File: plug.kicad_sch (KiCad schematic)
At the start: 27 parts, among them J1 KF2EDGR-3.81-2P, J10 Conn_01x02_XH2.54, J11 Conn_01x04_GH1.25, J3 KF2EDGR-3.81-2P, J4 KF2EDGR-3.81-2P, J5 Conn_01x04_GH1.25, J6 Conn_01x04_GH1.25, J7 Conn_01x02_XH2.54, J8 Conn_01x02_XH2.54, J9 Conn_01x02_XH2.54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

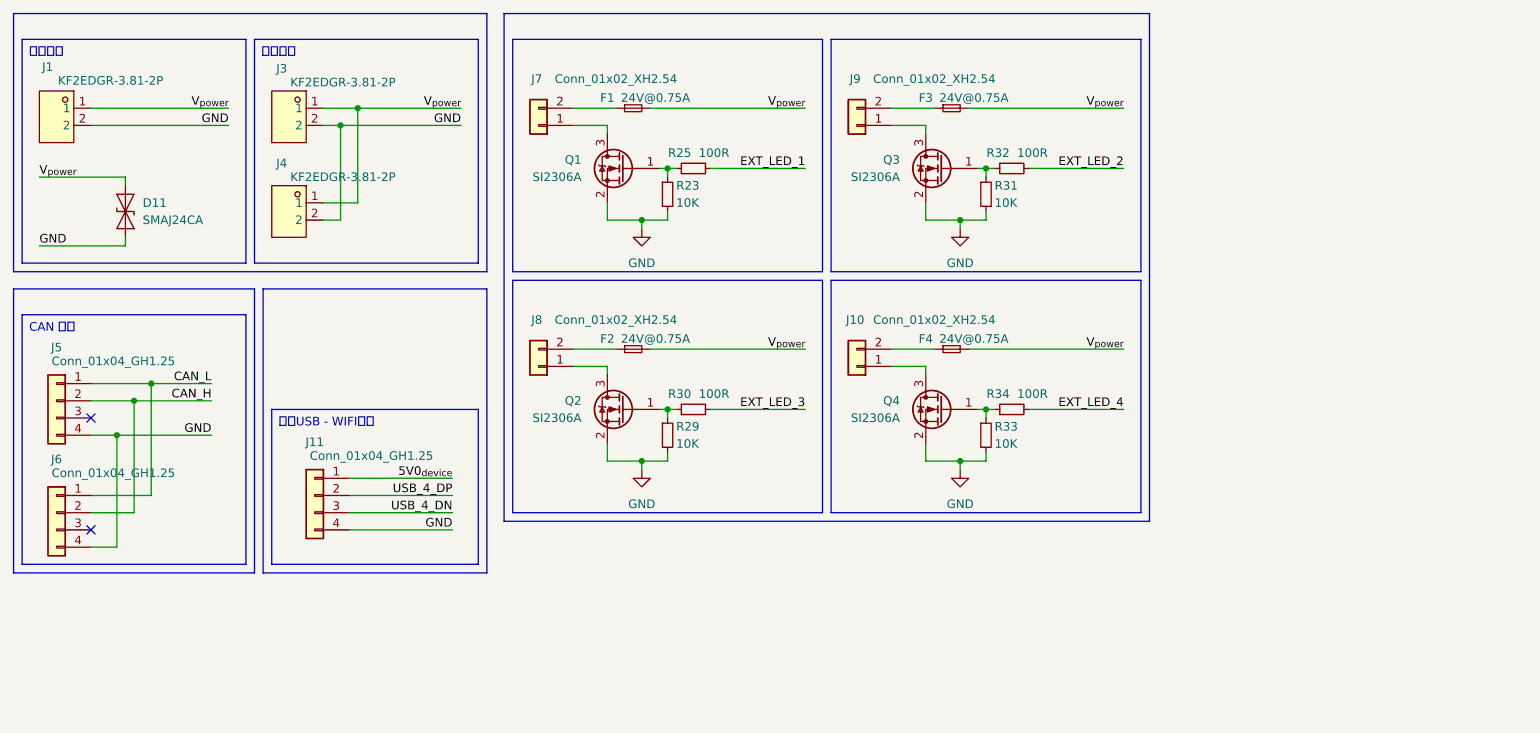
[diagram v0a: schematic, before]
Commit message: 暂存: 基本完成原理图(未分配封装，未ERC)
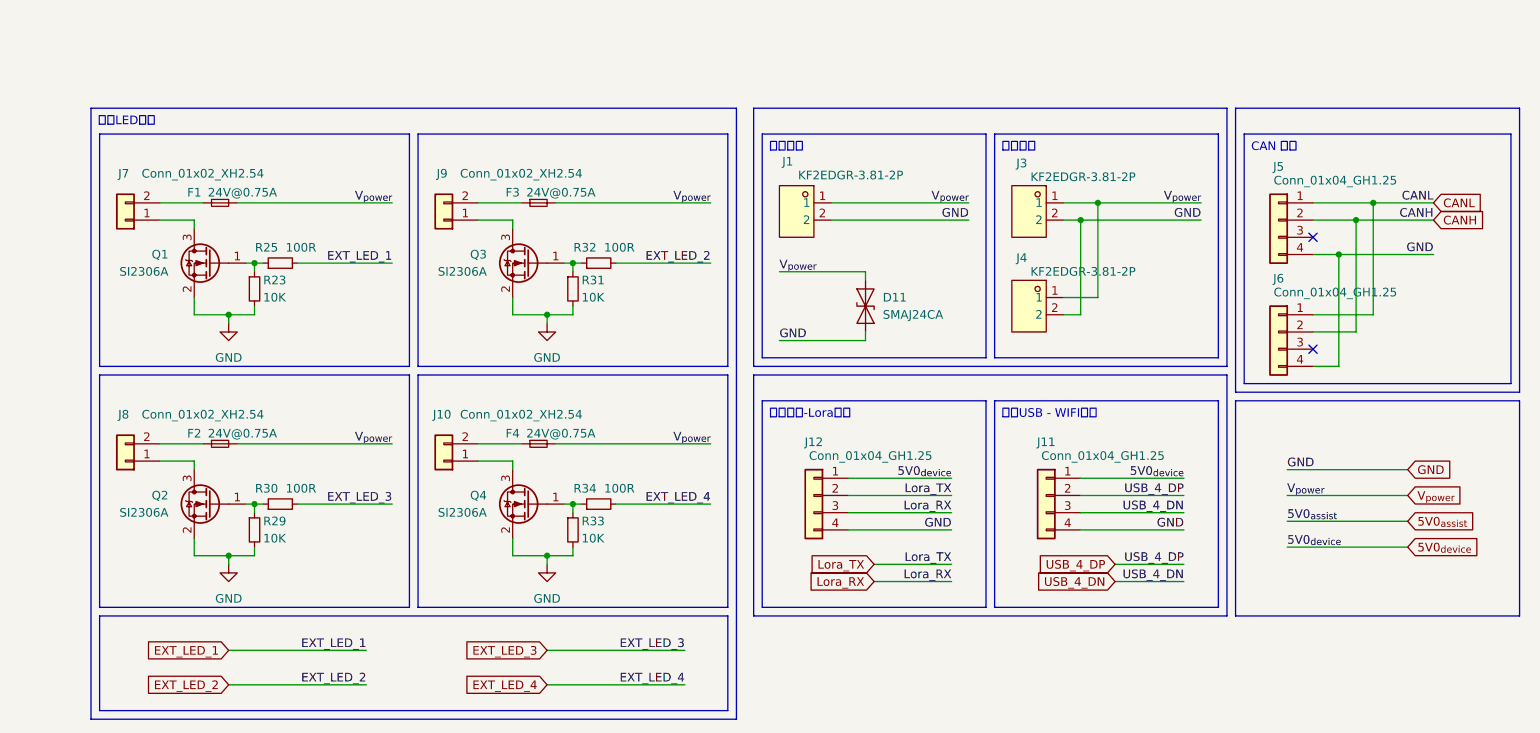
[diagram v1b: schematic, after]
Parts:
- added J12: Conn_01x04_GH1.25, symbol Connector_Generic:Conn_01x04
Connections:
- net 5V0_{device}: now also J12.1 (Pin_1)
- net GND: now also J12.4 (Pin_4)
- net CAN_H renamed CANH
- net CAN_L renamed CANL
- new net Lora_RX: J12.3 (Pin_3)
- new net Lora_TX: J12.2 (Pin_2)
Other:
- moved on the sheet: D11, F1, F2, F3, F4, J1, J10, J11, J3, J4, J5, J6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

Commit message: 暂存: 基本完成原理图(差雷达接口)
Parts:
- F1, F2, F3, F4: footprint (none) -> Fuse:Fuse_1812_4532Metric
- J10: renamed from J11; footprint (none) -> Connector_JST:JST_GH_SM04B-GHS-TB_1x04-1MP_P1.25mm_Horizontal
- J11: renamed from J5; footprint (none) -> Connector_JST:JST_GH_SM04B-GHS-TB_1x04-1MP_P1.25mm_Horizontal
- J12: renamed from J6; footprint (none) -> Connector_JST:JST_GH_SM04B-GHS-TB_1x04-1MP_P1.25mm_Horizontal
- J2: renamed from J7; footprint (none) -> Connector_JST:JST_XH_S2B-XH-A-1_1x02_P2.50mm_Horizontal
- J3: renamed from J8; footprint (none) -> Connector_JST:JST_XH_S2B-XH-A-1_1x02_P2.50mm_Horizontal
- J4: renamed from J9; footprint (none) -> Connector_JST:JST_XH_S2B-XH-A-1_1x02_P2.50mm_Horizontal
- J5: renamed from J10; footprint (none) -> Connector_JST:JST_XH_S2B-XH-A-1_1x02_P2.50mm_Horizontal
- J7: renamed from J12; footprint (none) -> Connector_JST:JST_GH_SM04B-GHS-TB_1x04-1MP_P1.25mm_Horizontal
- R26: renamed from R23; footprint (none) -> Resistor_SMD:R_0402_1005Metric
- R27: renamed from R29; footprint (none) -> Resistor_SMD:R_0402_1005Metric
- R28: renamed from R25; footprint (none) -> Resistor_SMD:R_0402_1005Metric
- R29: renamed from R30; footprint (none) -> Resistor_SMD:R_0402_1005Metric
- R30: renamed from R31; footprint (none) -> Resistor_SMD:R_0402_1005Metric
- R31: renamed from R33; footprint (none) -> Resistor_SMD:R_0402_1005Metric
- R32: footprint (none) -> Resistor_SMD:R_0402_1005Metric
- R33: renamed from R34; footprint (none) -> Resistor_SMD:R_0402_1005Metric
- renumbered J1 to J6, J3 to J8, J4 to J9
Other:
- note added: "补雷达接口及标签！！！"
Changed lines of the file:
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@@
+		)
+	)
+	(text "补雷达接口及标签！！！"
+		(exclude_from_sim no)
+		(at 49.53 32.004 0)
+		(effects
+			(font
+				(size 2.54 2.54)
+				(thickness 0.3175)
+				(color 255 0 0 1)
+			)
 		)
 	)
@@
 		(on_board yes)
 		(dnp no)
-		(property "Reference" "J6"
+		(property "Reference" "J12"
 			(at 205.74 60.706 0)
 			(effects
@@
 			)
 		)
-		(property "Footprint" ""
+		(property "Footprint" "Connector_JST:JST_GH_SM04B-GHS-TB_1x04-1MP_P1.25mm_Horizontal"
 			(at 205.74 68.58 0)
 			(effects
@@
 			(project "ZW1S"
 				(path "/c658c753-a869-4eb9-a520-6b2e7fae7fd9/cfdc2bd0-e52f-4e45-9f57-35a106e1bb09"
-					(reference "J6")
+					(reference "J12")
 					(unit 1)
 				)
@@
 		(dnp no)
 		(fields_autoplaced yes)
-		(property "Reference" "#PWR7"
+		(property "Reference" "#PWR13"
 			(at 50.8 73.66 0)
 			(effects
@@
 			(project ""
 				(path "/c658c753-a869-4eb9-a520-6b2e7fae7fd9/cfdc2bd0-e52f-4e45-9f57-35a106e1bb09"
-					(reference "#PWR7")
+					(reference "#PWR13")
 					(unit 1)
 				)
@@
 		(on_board yes)
 		(dnp no)
-		(property "Reference" "J7"
+		(property "Reference" "J2"
 			(at 35.306 45.212 0)
 			(effects
@@
 			)
 		)
-		(property "Footprint" ""
+		(property "Footprint" "Connector_JST:JST_XH_S2B-XH-A-1_1x02_P2.50mm_Horizontal"
 			(at 35.56 52.07 0)
 			(effects
@@
 			(project ""
 				(path "/c658c753-a869-4eb9-a520-6b2e7fae7fd9/cfdc2bd0-e52f-4e45-9f57-35a106e1bb09"
-					(reference "J7")
+					(reference "J2")
 					(unit 1)
 				)
@@
 		(on_board yes)
 		(dnp no)
-		(property "Reference" "J3"
+		(property "Reference" "J8"
 			(at 168.656 43.688 0)
 			(effects
@@
 			(project "ZW1S"
 				(path "/c658c753-a869-4eb9-a520-6b2e7fae7fd9/cfdc2bd0-e52f-4e45-9f57-35a106e1bb09"
-					(reference "J3")
+					(reference "J8")
 					(unit 1)
 				)
@@
 		(on_board yes)
 		(dnp no)
-		(property "Reference" "J4"
+		(property "Reference" "J9"
 			(at 168.656 57.658 0)
 			(effects
@@
 			(project "ZW1S"
 				(path "/c658c753-a869-4eb9-a520-6b2e7fae7fd9/cfdc2bd0-e52f-4e45-9f57-35a106e1bb09"
-					(reference "J4")
+					(reference "J9")
 					(unit 1)
 				)
@@
 		(on_board yes)
 		(dnp no)
-		(property "Reference" "R23"
+		(property "Reference" "R26"
 			(at 55.88 60.96 0)
 			(effects
@@
 			)
 		)
-		(property "Footprint" ""
+		(property "Footprint" "Resistor_SMD:R_0402_1005Metric"
 			(at 54.61 62.23 0)
 			(effects
@@
 			(project ""
 				(path "/c658c753-a869-4eb9-a520-6b2e7fae7fd9/cfdc2bd0-e52f-4e45-9f57-35a106e1bb09"
-					(reference "R23")
+					(reference "R26")
 					(unit 1)
 				)
@@
 		(on_board yes)
 		(dnp no)
-		(property "Reference" "J1"
+		(property "Reference" "J6"
 			(at 134.112 43.434 0)
 			(effects
@@
 			(project "ZW1S"
 				(path "/c658c753-a869-4eb9-a520-6b2e7fae7fd9/cfdc2bd0-e52f-4e45-9f57-35a106e1bb09"
-					(reference "J1")
+					(reference "J6")
 					(unit 1)
 				)
@@
 			)
 		)
-		(property "Footprint" ""
+		(property "Footprint" "Fuse:Fuse_1812_4532Metric"
 			(at 96.52 85.09 0)
 			(effects
@@
 			)
 		)
-		(property "Footprint" ""
+		(property "Footprint" "Fuse:Fuse_1812_4532Metric"
 			(at 49.53 85.09 0)
 			(effects
@@
 		(on_board yes)
 		(dnp no)
-		(property "Reference" "J11"
+		(property "Reference" "J10"
 			(at 171.45 84.836 0)
 			(effects
@@
 			)
 		)
-		(property "Footprint" ""
+		(property "Footprint" "Connector_JST:JST_GH_SM04B-GHS-TB_1x04-1MP_P1.25mm_Horizontal"
 			(at 171.45 92.71 0)
 			(effects
@@
 			(project "ZW1S"
 				(path "/c658c753-a869-4eb9-a520-6b2e7fae7fd9/cfdc2bd0-e52f-4e45-9f57-35a106e1bb09"
-					(reference "J11")
+					(reference "J10")
 					(unit 1)
 				)
@@
 		(on_board yes)
 		(dnp no)
-		(property "Reference" "J5"
+		(property "Reference" "J11"
 			(at 205.74 44.196 0)
 			(effects
@@
 			)
 		)
-		(property "Footprint" ""
+		(property "Footprint" "Connector_JST:JST_GH_SM04B-GHS-TB_1x04-1MP_P1.25mm_Horizontal"
 			(at 205.74 52.07 0)
 			(effects
@@
 			(project ""
 				(path "/c658c753-a869-4eb9-a520-6b2e7fae7fd9/cfdc2bd0-e52f-4e45-9f57-35a106e1bb09"
-					(reference "J5")
+					(reference "J11")
 					(unit 1)
 				)
@@
 		(on_board yes)
 		(dnp no)
-		(property "Reference" "R31"
+		(property "Reference" "R30"
 			(at 102.87 60.96 0)
 			(effects
@@
 			)
 		)
-		(property "Footprint" ""
+		(property "Footprint" "Resistor_SMD:R_0402_1005Metric"
 			(at 101.6 62.23 0)
 			(effects
@@
 			(project "ZW1S"
 				(path "/c658c753-a869-4eb9-a520-6b2e7fae7fd9/cfdc2bd0-e52f-4e45-9f57-35a106e1bb09"
-					(reference "R31")
+					(reference "R30")
 					(unit 1)
 				)
@@
 		(on_board yes)
 		(dnp no)
-		(property "Reference" "R30"
+		(property "Reference" "R29"
 			(at 56.388 91.694 90)
 			(effects
@@
 			)
 		)
-		(property "Footprint" ""
+		(property "Footprint" "Resistor_SMD:R_0402_1005Metric"
 			(at 58.42 93.98 0)
 			(effects
@@
 			(project "ZW1S"
 				(path "/c658c753-a869-4eb9-a520-6b2e7fae7fd9/cfdc2bd0-e52f-4e45-9f57-35a106e1bb09"
-					(reference "R30")
+					(reference "R29")
 					(unit 1)
 				)
@@
 			)
 		)
-		(property "Footprint" ""
+		(property "Footprint" "Resistor_SMD:R_0402_1005Metric"
 			(at 105.41 58.42 0)
 			(effects
@@
 		(on_board yes)
 		(dnp no)
-		(property "Reference" "R25"
+		(property "Reference" "R28"
 			(at 56.388 56.134 90)
 			(effects
@@
 			)
 		)
-		(property "Footprint" ""
+		(property "Footprint" "Resistor_SMD:R_0402_1005Metric"
 			(at 58.42 58.42 0)
 			(effects
@@
 			(project ""
 				(path "/c658c753-a869-4eb9-a520-6b2e7fae7fd9/cfdc2bd0-e52f-4e45-9f57-35a106e1bb09"
-					(reference "R25")
+					(reference "R28")
 					(unit 1)
 				)
@@
 		(on_board yes)
 		(dnp no)
-		(property "Reference" "R33"
+		(property "Reference" "R31"
 			(at 102.87 96.52 0)
 			(effects
@@
 			)
 		)
-		(property "Footprint" ""
+		(property "Footprint" "Resistor_SMD:R_0402_1005Metric"
 			(at 101.6 97.79 0)
 			(effects
@@
 			(project "ZW1S"
 				(path "/c658c753-a869-4eb9-a520-6b2e7fae7fd9/cfdc2bd0-e52f-4e45-9f57-35a106e1bb09"
-					(reference "R33")
+					(reference "R31")
 					(unit 1)
 				)
@@
 		(on_board yes)
 		(dnp no)
-		(property "Reference" "J9"
+		(property "Reference" "J4"
 			(at 82.296 45.212 0)
 			(effects
@@
 			)
 		)
-		(property "Footprint" ""
+		(property "Footprint" "Connector_JST:JST_XH_S2B-XH-A-1_1x02_P2.50mm_Horizontal"
 			(at 82.55 52.07 0)
 			(effects
@@
 			(project "ZW1S"
 				(path "/c658c753-a869-4eb9-a520-6b2e7fae7fd9/cfdc2bd0-e52f-4e45-9f57-35a106e1bb09"
-					(reference "J9")
+					(reference "J4")
 					(unit 1)
 				)
@@
 			)
 		)
-		(property "Footprint" ""
+		(property "Footprint" "Fuse:Fuse_1812_4532Metric"
 			(at 96.52 49.53 0)
 			(effects
@@
 		(dnp no)
 		(fields_autoplaced yes)
-		(property "Reference" "#PWR9"
+		(property "Reference" "#PWR14"
 			(at 50.8 109.22 0)
 			(effects
@@
 			(project "ZW1S"
 				(path "/c658c753-a869-4eb9-a520-6b2e7fae7fd9/cfdc2bd0-e52f-4e45-9f57-35a106e1bb09"
-					(reference "#PWR9")
+					(reference "#PWR14")
 					(unit 1)
 				)
@@
 		(on_board yes)
 		(dnp no)
-		(property "Reference" "R29"
+		(property "Reference" "R27"
 			(at 55.88 96.52 0)
 			(effects
@@
 			)
 		)
-		(property "Footprint" ""
+		(property "Footprint" "Resistor_SMD:R_0402_1005Metric"
 			(at 54.61 97.79 0)
 			(effects
@@
 			(project "ZW1S"
 				(path "/c658c753-a869-4eb9-a520-6b2e7fae7fd9/cfdc2bd0-e52f-4e45-9f57-35a106e1bb09"
-					(reference "R29")
+					(reference "R27")
 					(unit 1)
 				)
@@
 		(on_board yes)
 		(dnp no)
-		(property "Reference" "R34"
+		(property "Reference" "R33"
 			(at 103.378 91.694 90)
 			(effects
@@
 			)
 		)
-		(property "Footprint" ""
+		(property "Footprint" "Resistor_SMD:R_0402_1005Metric"
 			(at 105.41 93.98 0)
 			(effects
@@
 			(project "ZW1S"
 				(path "/c658c753-a869-4eb9-a520-6b2e7fae7fd9/cfdc2bd0-e52f-4e45-9f57-35a106e1bb09"
-					(reference "R34")
+					(reference "R33")
 					(unit 1)
 				)
@@
 		(on_board yes)
 		(dnp no)
-		(property "Reference" "J12"
+		(property "Reference" "J7"
 			(at 137.16 84.836 0)
 			(effects
@@
 			)
 		)
-		(property "Footprint" ""
+		(property "Footprint" "Connector_JST:JST_GH_SM04B-GHS-TB_1x04-1MP_P1.25mm_Horizontal"
 			(at 137.16 92.71 0)
 			(effects
@@
 			(project "ZW1S"
 				(path "/c658c753-a869-4eb9-a520-6b2e7fae7fd9/cfdc2bd0-e52f-4e45-9f57-35a106e1bb09"
-					(reference "J12")
+					(reference "J7")
 					(unit 1)
 				)
@@
 		(on_board yes)
 		(dnp no)
-		(property "Reference" "J10"
+		(property "Reference" "J5"
 			(at 82.296 80.772 0)
 			(effects
@@
 			)
 		)
-		(property "Footprint" ""
+		(property "Footprint" "Connector_JST:JST_XH_S2B-XH-A-1_1x02_P2.50mm_Horizontal"
 			(at 82.55 87.63 0)
 			(effects
@@
 			(project "ZW1S"
 				(path "/c658c753-a869-4eb9-a520-6b2e7fae7fd9/cfdc2bd0-e52f-4e45-9f57-35a106e1bb09"
-					(reference "J10")
+					(reference "J5")
 					(unit 1)
 				)
@@
 			)
 		)
-		(property "Footprint" ""
+		(property "Footprint" "Fuse:Fuse_1812_4532Metric"
 			(at 49.53 49.53 0)
 			(effects
@@
 		(on_board yes)
 		(dnp no)
-		(property "Reference" "J8"
+		(property "Reference" "J3"
 			(at 35.306 80.772 0)
 			(effects
@@
 			)
 		)
-		(property "Footprint" ""
+		(property "Footprint" "Connector_JST:JST_XH_S2B-XH-A-1_1x02_P2.50mm_Horizontal"
 			(at 35.56 87.63 0)
 			(effects
@@
 			(project "ZW1S"
 				(path "/c658c753-a869-4eb9-a520-6b2e7fae7fd9/cfdc2bd0-e52f-4e45-9f57-35a106e1bb09"
-					(reference "J8")
-					(unit 1)
-				)
+					(reference "J3")
+					(unit 1)
+				)

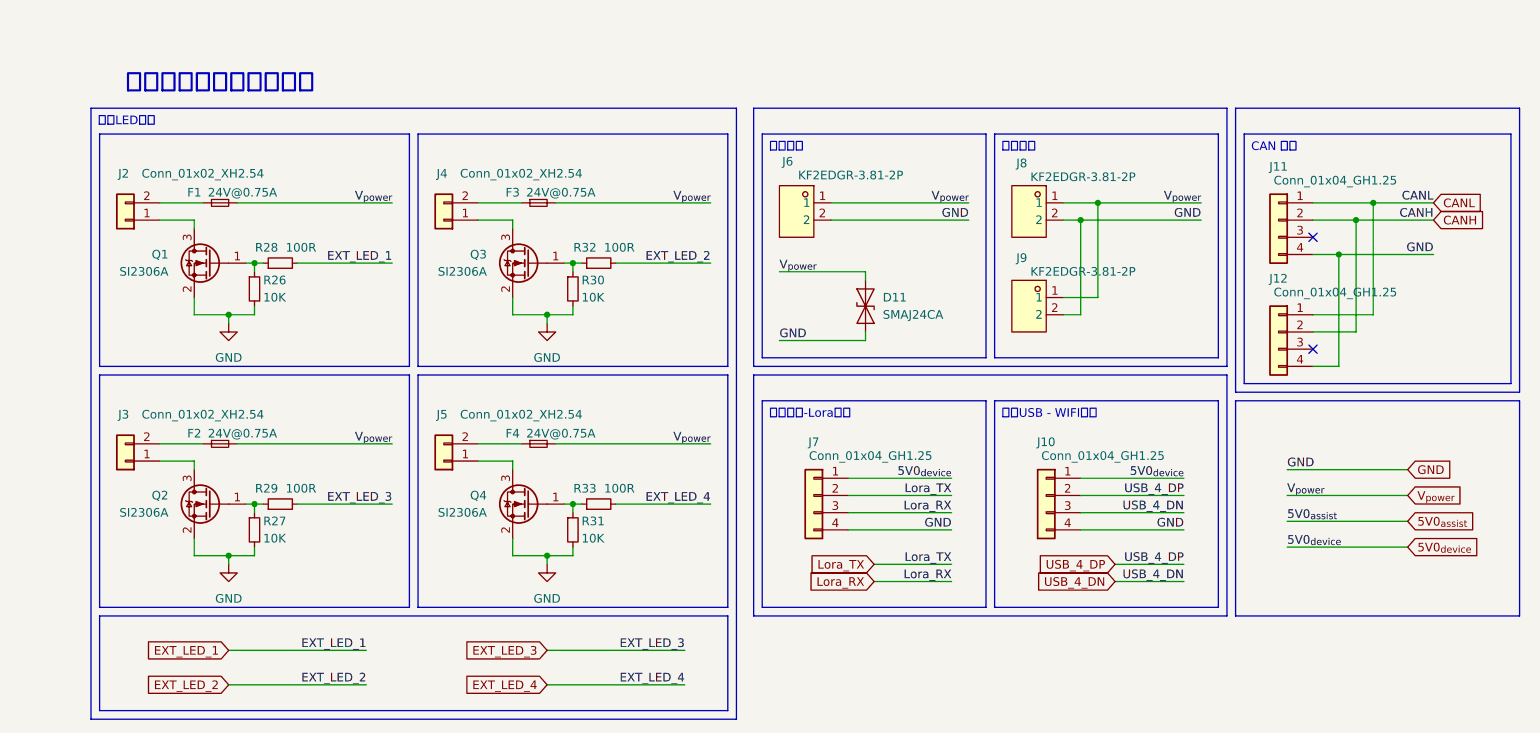
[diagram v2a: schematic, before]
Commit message: 暂存: 布局布线基本完成(DRC未过，GND不全)
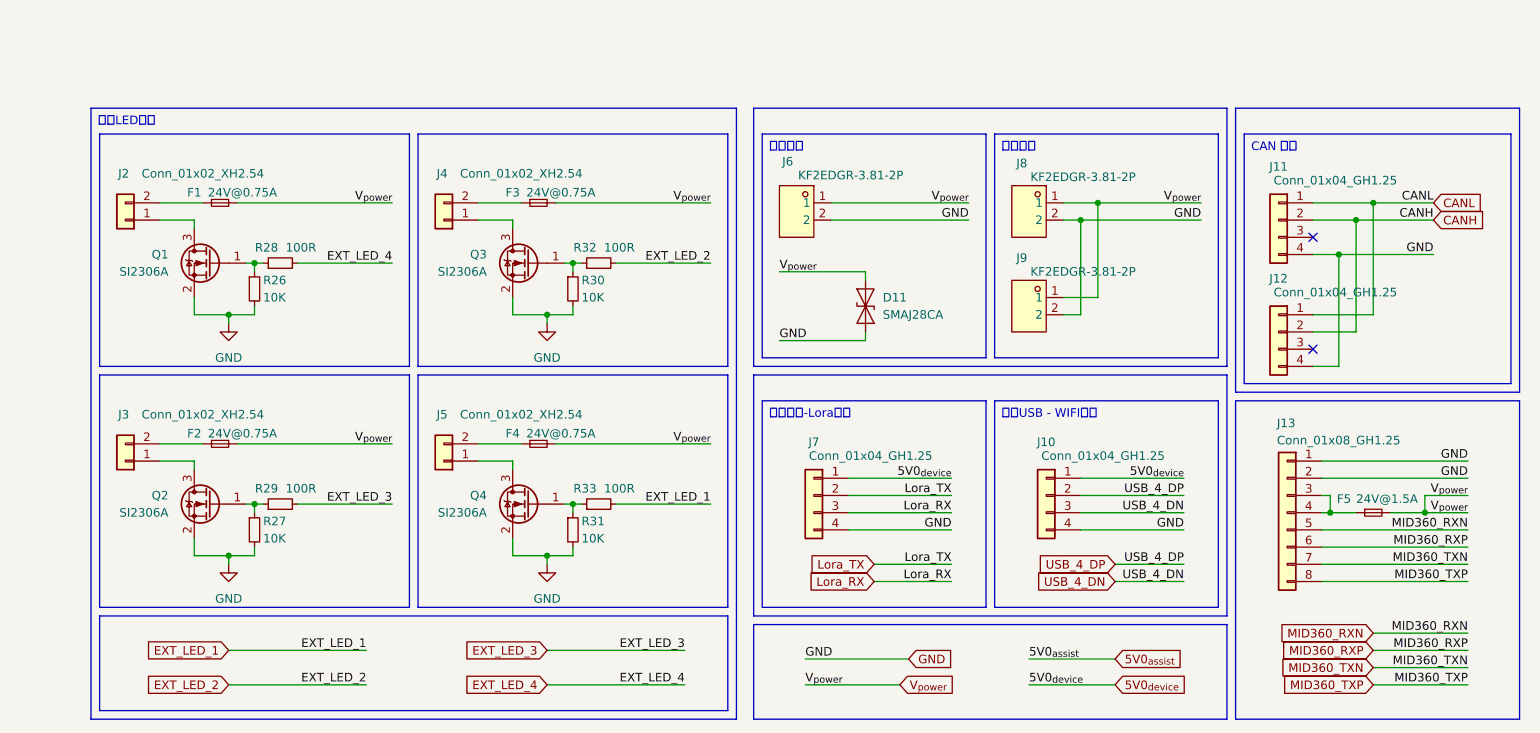
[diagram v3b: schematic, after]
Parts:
- added F5: 24V@1.5A, Fuse:Fuse_1812_4532Metric, symbol Device:Fuse_Small
- added J13: Conn_01x08_GH1.25, Connector_JST:JST_GH_SM08B-GHS-TB_1x08-1MP_P1.25mm_Horizontal, symbol Connector_Generic:Conn_01x08
- D11: value SMAJ24CA -> SMAJ28CA
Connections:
- net EXT_LED_1: now also R33.2; no longer R28.2
- net EXT_LED_4: now also R28.2; no longer R33.2
- net GND: now also J13.1 (Pin_1), J13.2 (Pin_2)
- net V_{power}: now also F5.2
- new net: F5.1, J13.3 (Pin_3), J13.4 (Pin_4)
- new net MID360_RXN: J13.5 (Pin_5)
- new net MID360_RXP: J13.6 (Pin_6)
- new net MID360_TXN: J13.7 (Pin_7)
- new net MID360_TXP: J13.8 (Pin_8)
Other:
- note removed: "补雷达接口及标签！！！"
